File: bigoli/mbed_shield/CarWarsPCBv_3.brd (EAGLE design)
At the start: 69.3 x 64.2 mm, 27 parts, among them J1 MAGJACK, X1 E-STOP, X2 NEOPIXEL, X3 ENCODER, X4 STEER_POT, X5 STEER, X6 OSMC

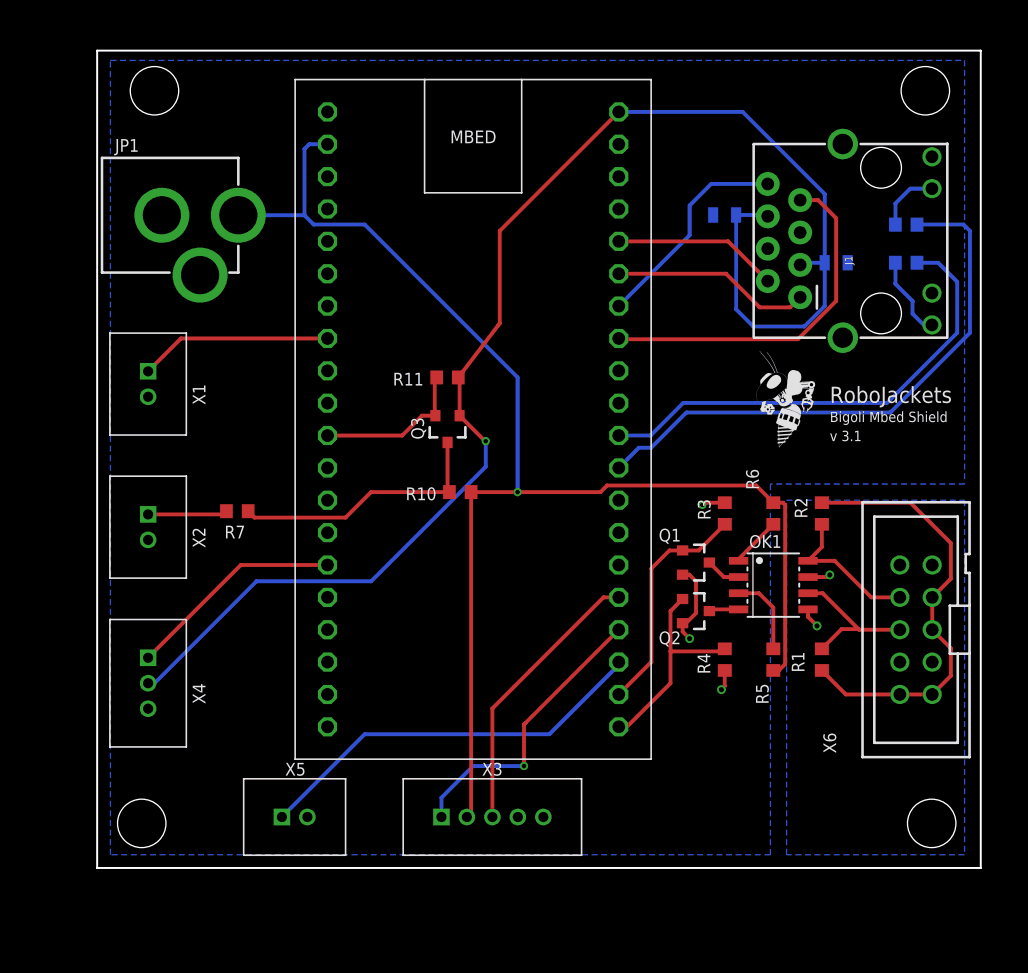
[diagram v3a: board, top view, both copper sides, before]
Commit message: Cleaned up library, re-routed new connectors
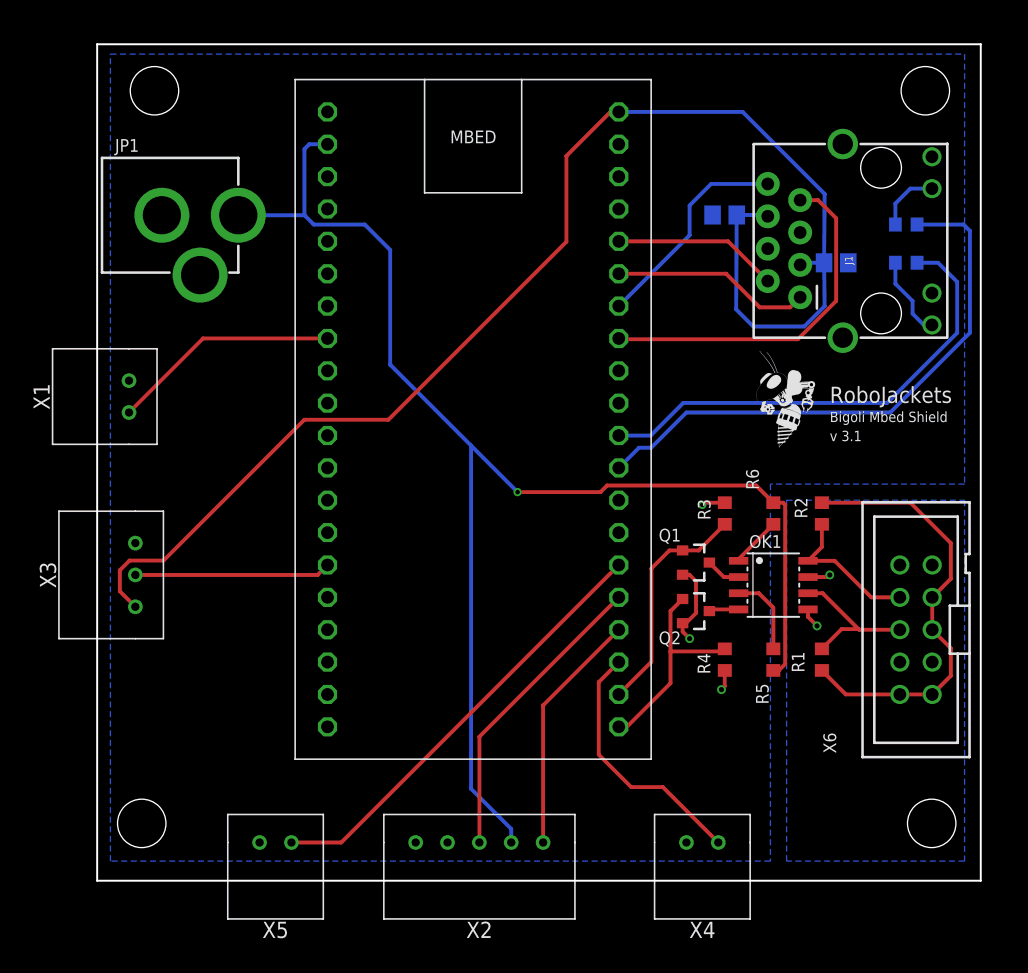
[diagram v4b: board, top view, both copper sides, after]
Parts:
- removed Q3: (no value), SparkFun-DiscreteSemi:SOT23-3
- removed R10, R11: 10k, rcl:R0603
- removed R7: 340, rcl:R0603
- C1, C2: device SparkFun-Capacitors:0805 -> rcl:C0805
- X1: device RoboJackets-Connectors:2MM-2-V -> CarWarsPCBv_3:S2B-EH
- X2: value NEOPIXEL -> ENCODER; device RoboJackets-Connectors:2MM-2-V -> CarWarsPCBv_3:S5B-EH
- X3: value ENCODER -> STEER ANGLE; device RoboJackets-Connectors:2MM-5-V -> CarWarsPCBv_3:S3B-EH
- X4: value STEER_POT -> STEER PWM; device RoboJackets-Connectors:2MM-3-V -> CarWarsPCBv_3:S2B-EH
- X5: value STEER -> BRAKE PWM; device RoboJackets-Connectors:2MM-2-V -> CarWarsPCBv_3:S2B-EH
- moved X4 45.3 mm to (47.5, 2.00), turned to 180 degrees
- moved X2 35.9 mm to (30.0, 2.00), turned to 180 degrees
- moved X3 33.9 mm to (3.00, 23.0), turned to 90 degrees
- moved X5 2.50 mm to (14.0, 2.00), turned to 180 degrees
- moved X1 1.79 mm to (2.50, 37.0), turned to 90 degrees
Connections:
- removed net N$7: Q3.3, R10.2, R7.1
- removed net NEOPIXEL_CONTROL: MBED.11, Q3.2, R11.2
- removed net NEO_INPUT: R7.2, X2.1
- new net BRAKE_PWM: MBED.26, X5.1
- net +3V3: now also X3.1; no longer Q3.1, R11.1, X4.2
- net +5V: now also X2.2; no longer R10.1, X3.2
- net ENC_A: now also X2.3; no longer X3.3
- net ENC_B: now also X2.1; no longer X3.1
- net GND: now also X2.5, X3.3, X4.2; no longer X2.2, X3.5, X4.3
- net STEER_POT: now also X3.2; no longer X4.1
- net STEER_PWM: now also X4.1; no longer X5.1
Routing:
- net BRAKE_PWM: track 0.00 -> 34.7 mm
- net N$7: track 20.8 -> 0.00 mm
- net NEOPIXEL_CONTROL: track 12.2 -> 0.00 mm
- net STEER_PWM: track 31.6 -> 20.2 mm
- net NEO_INPUT: track 6.25 -> 0.00 mm
- net +3V3: track 115.0 -> 109.0 mm, vias 1 -> 0
- net ENC_B: track 22.8 -> 19.2 mm, vias 1 -> 0
- net +5V: track 108.1 -> 111.3 mm
- net E-STOP_STATUS: track 15.1 -> 18.0 mm
- net ENC_A: track 22.1 -> 23.8 mm
- net STEER_POT: track 17.1 -> 15.4 mm
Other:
- board size 69.3 x 64.2 mm -> 69.3 x 65.7 mm

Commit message: Curved the board edges, cleaned up hole placement
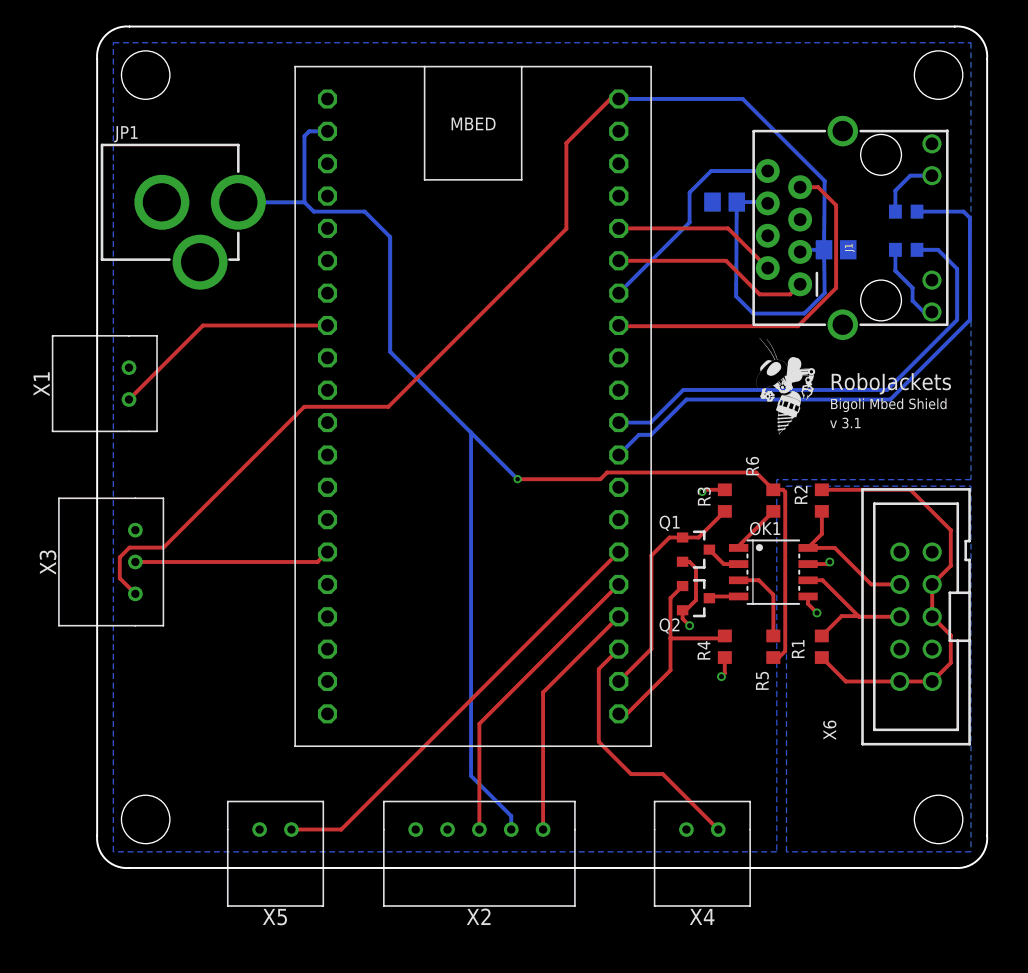
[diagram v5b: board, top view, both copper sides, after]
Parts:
- moved J1 1.02 mm to (72.6, 42.6)
- moved JP1 1.02 mm to (-2.62, 52.2)
- moved MBED 1.02 mm to (29.5, 37.5)
- moved OK1 1.02 mm to (53.1, 23.2)
- moved Q1 1.02 mm to (47.0, 25.0)
- moved X6 1.02 mm to (64.3, 19.7)
- moved X2 1.02 mm to (30.0, 3.02)
- moved X4 1.02 mm to (47.5, 3.02)
- moved X5 1.02 mm to (14.0, 3.02)
- moved C1 1.02 mm to (49.2, 52.3)
- moved C2 1.02 mm to (58.0, 48.5)
- moved Q2 1.02 mm to (47.0, 21.2)
- moved R1 1.02 mm to (56.9, 17.4)
- moved R2 1.02 mm to (56.9, 28.8)
- moved R3 1.02 mm to (49.3, 28.8)
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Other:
- board size 69.3 x 65.7 mm -> 69.9 x 66.1 mm

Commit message: Added gerbers, generated image
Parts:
- removed R9: 47, rcl:R0603
- added R7: 47, rcl:R0603
- added U$2: (no value), RoboJackets-Aesthetics:ROBOJACKETS
- JP1: value POWER_JACK -> 5V POWER
- moved U$1 6.35 mm to (47.1, 34.0)
- moved R8 3.00 mm to (63.5, 51.5)
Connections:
- net ETH_LED_G: now also R8.2; no longer R9.2
- net ETH_LED_Y: now also R7.2; no longer R8.2
- net N$6: now also R7.1; no longer R8.1
- net N$8: now also R8.1; no longer R9.1
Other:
- board text added: "v 3.2"
- board text removed: "RoboJackets"
- board text removed: "v 3.1"

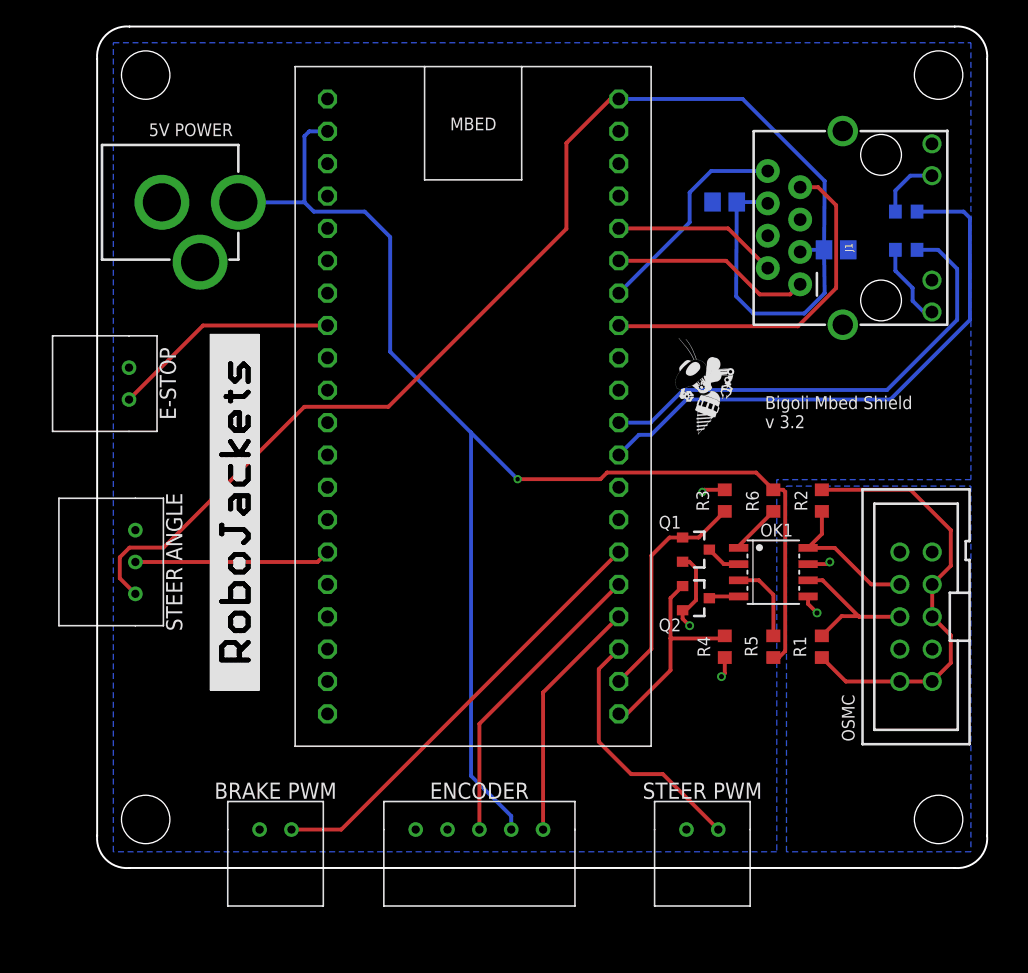
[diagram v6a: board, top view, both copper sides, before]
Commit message: Fixed connector solder vias and generated gerbers
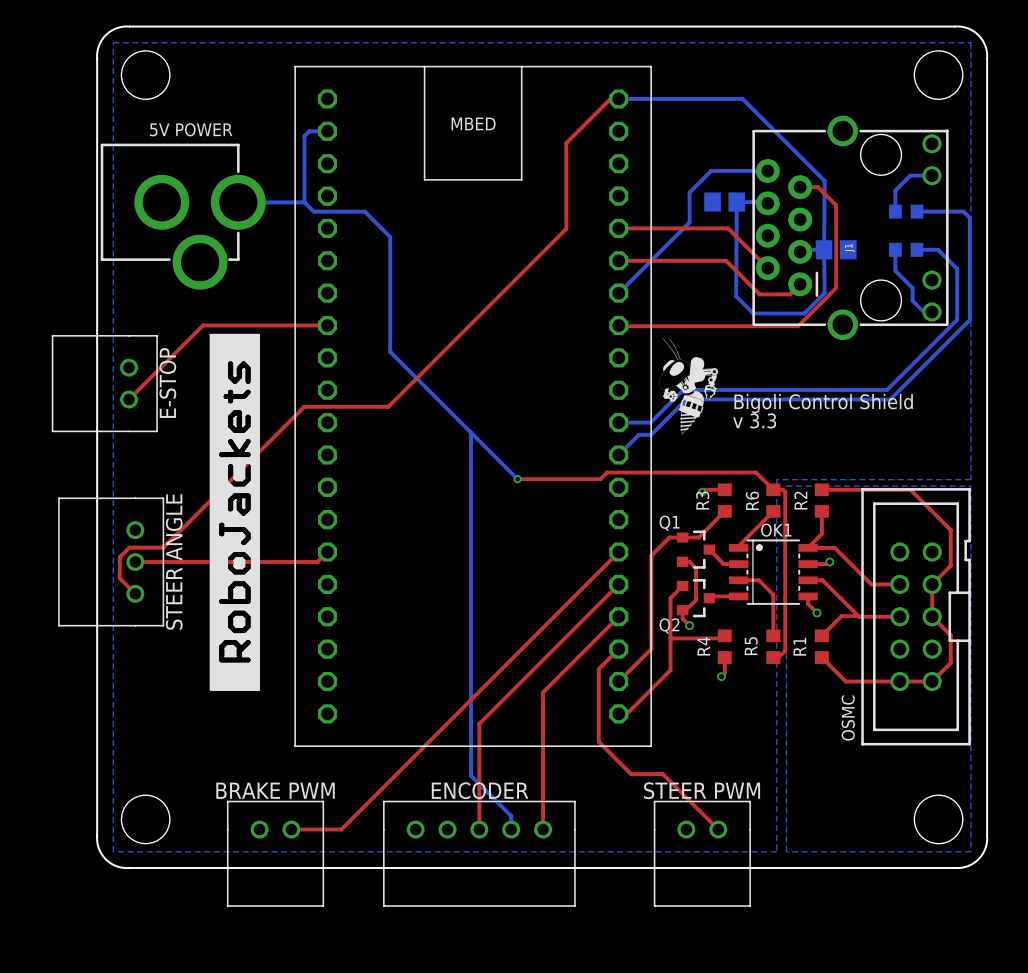
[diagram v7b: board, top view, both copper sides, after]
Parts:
- moved U$1 1.27 mm to (45.9, 34.0)
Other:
- board text added: "Bigoli Control Shield"
- board text added: "v 3.3"
- board text removed: "Bigoli Mbed Shield"
- board text removed: "v 3.2"
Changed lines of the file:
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@@
 <hole x="66.04" y="62.23" drill="3.8"/>
 <hole x="66.04" y="3.81" drill="3.8"/>
-<text x="52.42" y="36.016" size="1.016" layer="21" font="vector" ratio="15">Bigoli Mbed Shield</text>
-<text x="52.42" y="34.516" size="1.016" layer="21" font="vector" ratio="15">v 3.2</text>
+<text x="49.88" y="36.016" size="1.143" layer="21" font="vector" ratio="15">Bigoli Control Shield</text>
+<text x="49.88" y="34.516" size="1.143" layer="21" font="vector" ratio="15">v 3.3</text>
 <wire x1="67.31" y1="0" x2="2.54" y2="0" width="0.1524" layer="20"/>
 <wire x1="0" y1="2.54" x2="0" y2="63.5" width="0.1524" layer="20"/>
@@
 <attribute name="SPICEPREFIX" value="R" x="53.07" y="28.836" size="1.778" layer="27" rot="R90" display="off"/>
 </element>
-<element name="U$1" library="RoboJackets-Aesthetics" package="ROBOBUZZ_0.4X" value="" x="47.15" y="34.016"/>
+<element name="U$1" library="RoboJackets-Aesthetics" package="ROBOBUZZ_0.4X" value="" x="45.88" y="34.016"/>
 <element name="C2" library="rcl" library_urn="urn:adsk.eagle:library:334" package="C0805" package3d_urn="urn:adsk.eagle:package:23617/2" value="1uF" x="58" y="48.516" smashed="yes" rot="MR180">
 <attribute name="NAME" x="57.365" y="47.0635" size="1" layer="26" rot="MR180"/>
